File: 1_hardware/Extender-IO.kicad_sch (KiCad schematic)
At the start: 8 parts, among them U10 PCA9555PW,118, U11 PCA9555PW,118, U4 PCA9555PW,118, U5 PCA9555PW,118, U6 PCA9555PW,118, U7 PCA9555PW,118, U8 PCA9555PW,118, U9 PCA9555PW,118

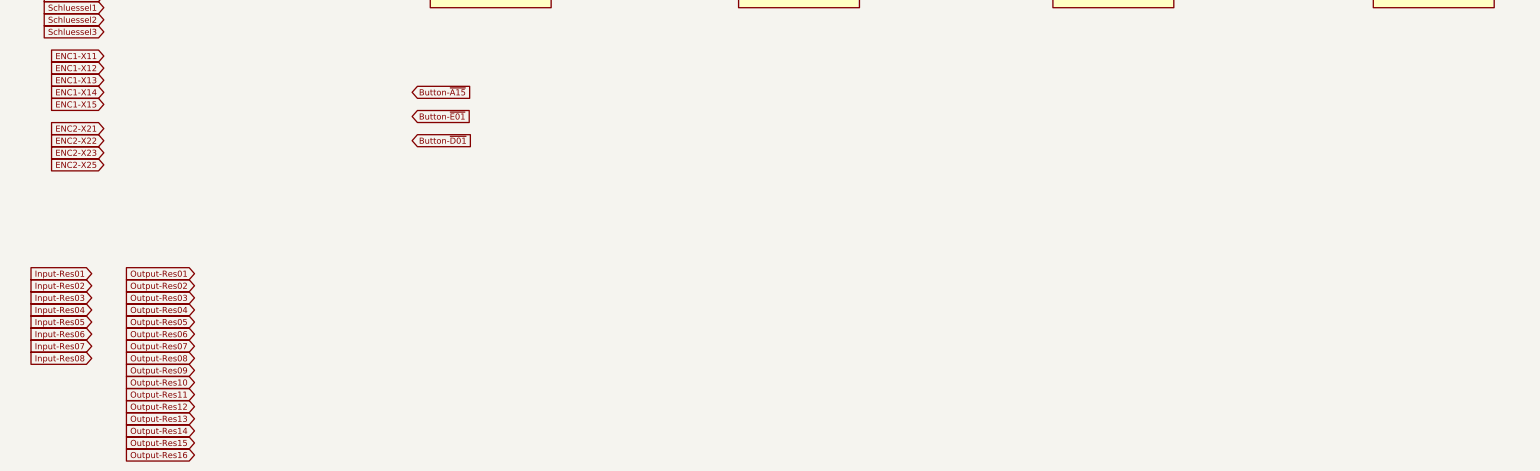
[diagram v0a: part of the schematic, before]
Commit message: finished most of schematic, init STM32 program
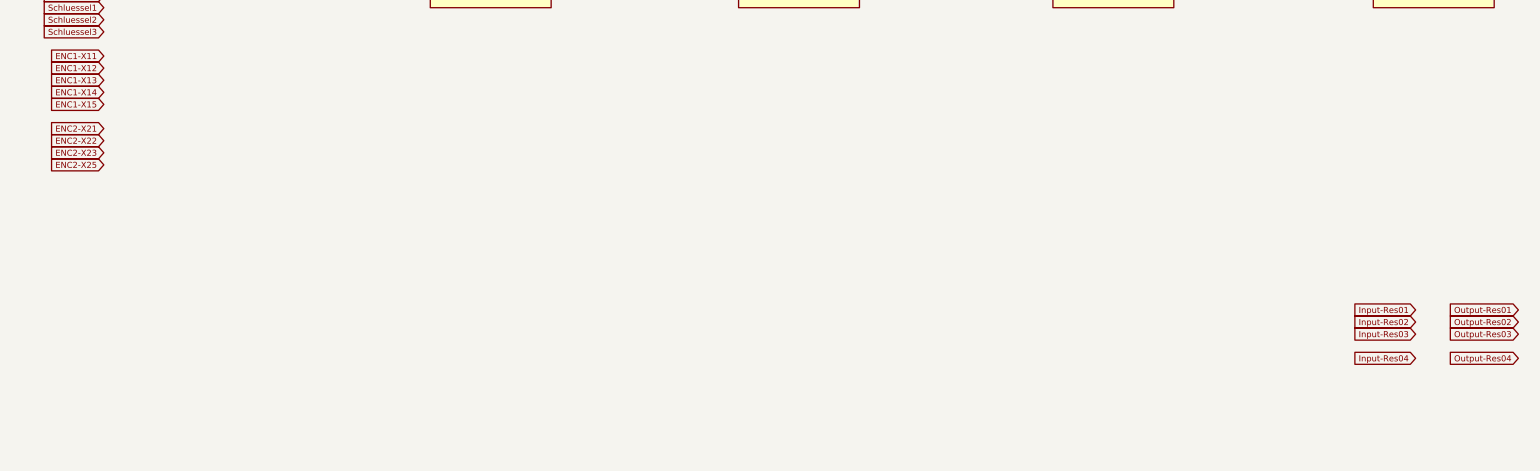
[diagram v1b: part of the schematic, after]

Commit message: finished schematics and board
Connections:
- net Button-A01: now also U9.10 (IO0_6)
- net Button-A02: now also U9.20 (IO1_7)
- net Button-A03: now also U9.19 (IO1_6)
- net Button-A04: now also U9.8 (IO0_4)
- net Button-A05: now also U9.17 (IO1_4)
- net Button-A06: now also U9.5 (IO0_1)
- net Button-A07: now also U9.6 (IO0_2)
- net Button-A08: now also U9.7 (IO0_3)
- net Button-A09: now also U9.9 (IO0_5)
- net Button-A10: now also U9.4 (IO0_0)
- net Button-A11: now also U9.11 (IO0_7)
- net Button-A12: now also U9.15 (IO1_2)
- net Button-A13: now also U10.17 (IO1_4)
- net Button-A14: now also U10.14 (IO1_1)
- net Button-A16: now also U10.5 (IO0_1)
- net Button-B01: now also U6.19 (IO1_6)
- net Button-B02: now also U6.18 (IO1_5)
- net Button-B03: now also U6.16 (IO1_3)
- net Button-B04: now also U6.14 (IO1_1)
- net Button-B05: now also U6.10 (IO0_6)
- net Button-B06: now also U6.8 (IO0_4)
- net Button-B07: now also U6.6 (IO0_2)
- net Button-B08: now also U6.4 (IO0_0)
- net Button-B09: now also U6.17 (IO1_4)
- net Button-B10: now also U6.15 (IO1_2)
- net Button-B11: now also U6.13 (IO1_0)
- net Button-B12: now also U6.11 (IO0_7)
- net Button-B13: now also U6.9 (IO0_5)
- net Button-B14: now also U6.7 (IO0_3)
- net Button-B15: now also U6.5 (IO0_1)
- net Button-C01: now also U5.10 (IO0_6)
- net Button-C02: now also U5.20 (IO1_7)
- net Button-C03: now also U5.19 (IO1_6)
- net Button-C04: now also U5.8 (IO0_4)
- net Button-C05: now also U5.17 (IO1_4)
- net Button-C06: now also U5.5 (IO0_1)
- net Button-C07: now also U5.6 (IO0_2)
- net Button-C08: now also U5.7 (IO0_3)
- net Button-C09: now also U5.9 (IO0_5)
- net Button-C10: now also U5.4 (IO0_0)
- net Button-C11: now also U5.11 (IO0_7)
- net Button-C12: now also U5.15 (IO1_2)
- net Button-C13: now also U5.16 (IO1_3)
- net Button-C14: now also U5.14 (IO1_1)
- net Button-C15: now also U5.18 (IO1_5)
- net Button-D02: now also U10.10 (IO0_6)
- net Button-E02: now also U10.8 (IO0_4)
- net ENC1-X11: now also U10.4 (IO0_0)
- net ENC1-X12: now also U10.6 (IO0_2)
- net ENC1-X13: now also U10.9 (IO0_5)
- net ENC1-X14: now also U10.11 (IO0_7)
- net ENC1-X15: now also U10.7 (IO0_3)
- net ENC2-X21: now also U9.13 (IO1_0)
- net ENC2-X22: now also U9.14 (IO1_1)
- net ENC2-X23: now also U9.18 (IO1_5)
- net ENC2-X25: now also U9.16 (IO1_3)
- net Input-Res01: now also U7.13 (IO1_0)
- net Input-Res02: now also U7.14 (IO1_1)
- net Input-Res03: now also U7.15 (IO1_2)
- net Input-Res04: now also U7.16 (IO1_3)
- net LED-A01: now also U8.7 (IO0_3)
- net LED-A02: now also U8.16 (IO1_3)
- net LED-A03: now also U8.15 (IO1_2)
- net LED-A04: now also U8.6 (IO0_2)
- net LED-A05: now also U8.14 (IO1_1)
- net LED-A06: now also U8.8 (IO0_4)
- net LED-A07: now also U8.5 (IO0_1)
- net LED-A08: now also U8.9 (IO0_5)
- net LED-A09: now also U8.10 (IO0_6)
- net LED-A10: now also U8.4 (IO0_0)
- net LED-A11: now also U8.11 (IO0_7)
- net LED-A12: now also U8.13 (IO1_0)
- net LED-A14: now also U11.6 (IO0_2)
- net LED-A15: now also U8.17 (IO1_4)
- net LED-A16: now also U8.18 (IO1_5)
- net LED-B01: now also U7.11 (IO0_7)
- net LED-B02: now also U7.10 (IO0_6)
- net LED-B03: now also U7.9 (IO0_5)
- net LED-B04: now also U7.8 (IO0_4)
- net LED-B05: now also U7.7 (IO0_3)
- net LED-B06: now also U7.6 (IO0_2)
- net LED-B07: now also U7.5 (IO0_1)
- net LED-B08: now also U7.4 (IO0_0)
- net LED-B09: now also U4.20 (IO1_7)
- net LED-B10: now also U4.19 (IO1_6)
- net LED-B11: now also U4.18 (IO1_5)
- net LED-B12: now also U4.17 (IO1_4)
- net LED-B13: now also U4.16 (IO1_3)
- net LED-B14: now also U4.15 (IO1_2)
- net LED-B15: now also U4.14 (IO1_1)
- net LED-C01: now also U11.10 (IO0_6)
- net LED-C02: now also U4.13 (IO1_0)
- net LED-C03: now also U4.11 (IO0_7)
- net LED-C04: now also U11.9 (IO0_5)
- net LED-C05: now also U4.10 (IO0_6)
- net LED-C06: now also U4.5 (IO0_1)
- net LED-C07: now also U11.8 (IO0_4)
- net LED-C08: now also U4.6 (IO0_2)
- net LED-C09: now also U4.7 (IO0_3)
- net LED-C10: now also U11.7 (IO0_3)
- net LED-C11: now also U4.8 (IO0_4)
- net LED-C12: now also U4.9 (IO0_5)
- net LED-C13: now also U11.11 (IO0_7)
- net LED-C15: now also U4.4 (IO0_0)
- net LED-D01: now also U11.4 (IO0_0)
- net LED-D02: now also U11.5 (IO0_1)
- net LED-E01: now also U8.19 (IO1_6)
- net LED-E02: now also U8.20 (IO1_7)
- net Output-Res01: now also U7.17 (IO1_4)
- net Output-Res02: now also U7.18 (IO1_5)
- net Output-Res03: now also U7.19 (IO1_6)
- net Output-Res04: now also U7.20 (IO1_7)
- net Schluessel0: now also U10.15 (IO1_2)
- net Schluessel1: now also U5.13 (IO1_0)
- net Schluessel2: now also U10.13 (IO1_0)
- net Schluessel3: now also U10.16 (IO1_3)
- net EXP_INT1: now reaches U4.1 (~{INT})
- net GND: now reaches U4.12 (VSS)
- net GND: now also U10.12 (VSS), U10.21 (A0), U10.3 (A2), U11.12 (VSS), U11.3 (A2), U4.2 (A1), U4.21 (A0), U5.12 (VSS), U5.2 (A1), U6.12 (VSS), U6.21 (A0), U7.12 (VSS), U8.12 (VSS), U8.2 (A1), U8.21 (A0), U8.3 (A2), U9.12 (VSS), U9.2 (A1), U9.3 (A2)
- net +3V3: now reaches U4.24 (VDD)
- net +3V3: now also U10.2 (A1), U10.24 (VDD), U11.2 (A1), U11.21 (A0), U11.24 (VDD), U4.3 (A2), U5.21 (A0), U5.24 (VDD), U5.3 (A2), U6.2 (A1), U6.24 (VDD), U6.3 (A2), U7.2 (A1), U7.21 (A0), U7.24 (VDD), U7.3 (A2), U8.24 (VDD), U9.21 (A0), U9.24 (VDD)
- net EXP_INT2: now reaches U5.1 (~{INT})
- net EXP_INT4: now reaches U7.1 (~{INT})
- net EXP_INT5: now reaches U8.1 (~{INT})
- net EXP_INT7: now reaches U10.1 (~{INT})
- net EXP_INT8: now reaches U11.1 (~{INT})
- net EXP_INT6: now reaches U9.1 (~{INT})
- net EXP_INT3: now reaches U6.1 (~{INT})
- no-connect marks 0 -> 12

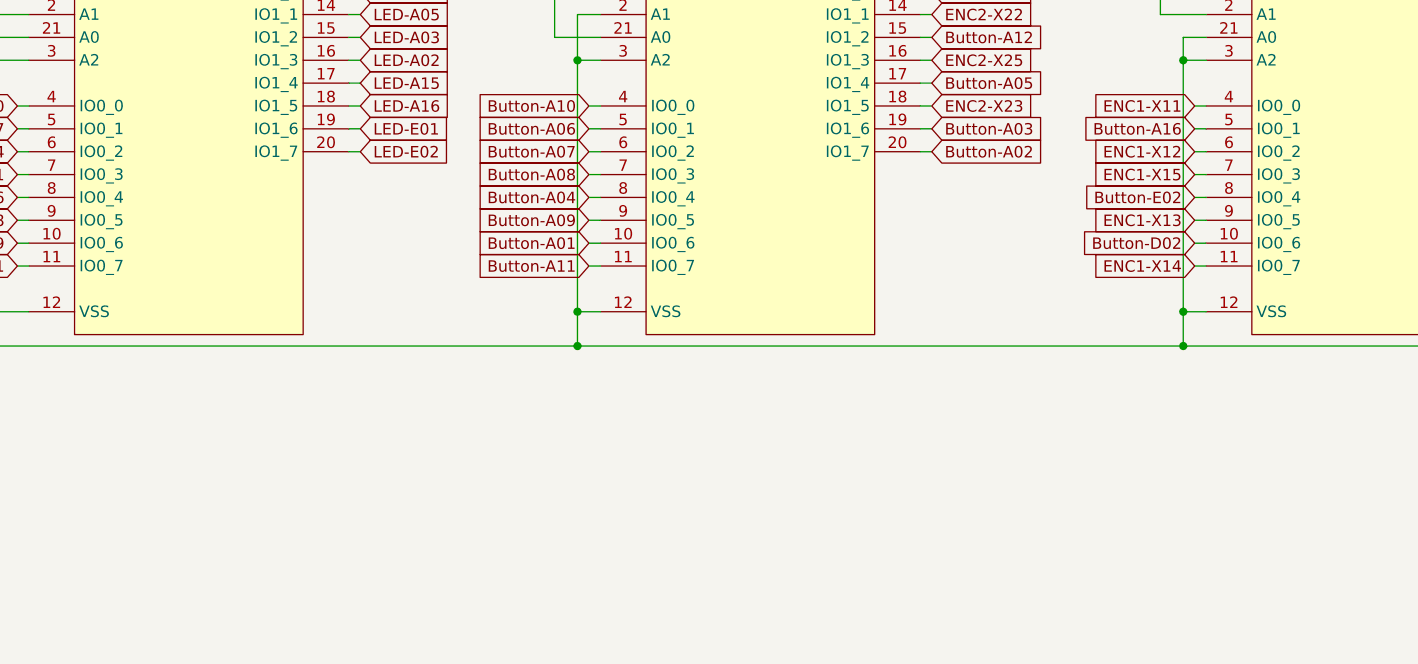
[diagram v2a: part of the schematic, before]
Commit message: changed from STM32F103C8 over to STM32L151C8 changed controller pinout, minor tweaks in board design, added labels and debug pads
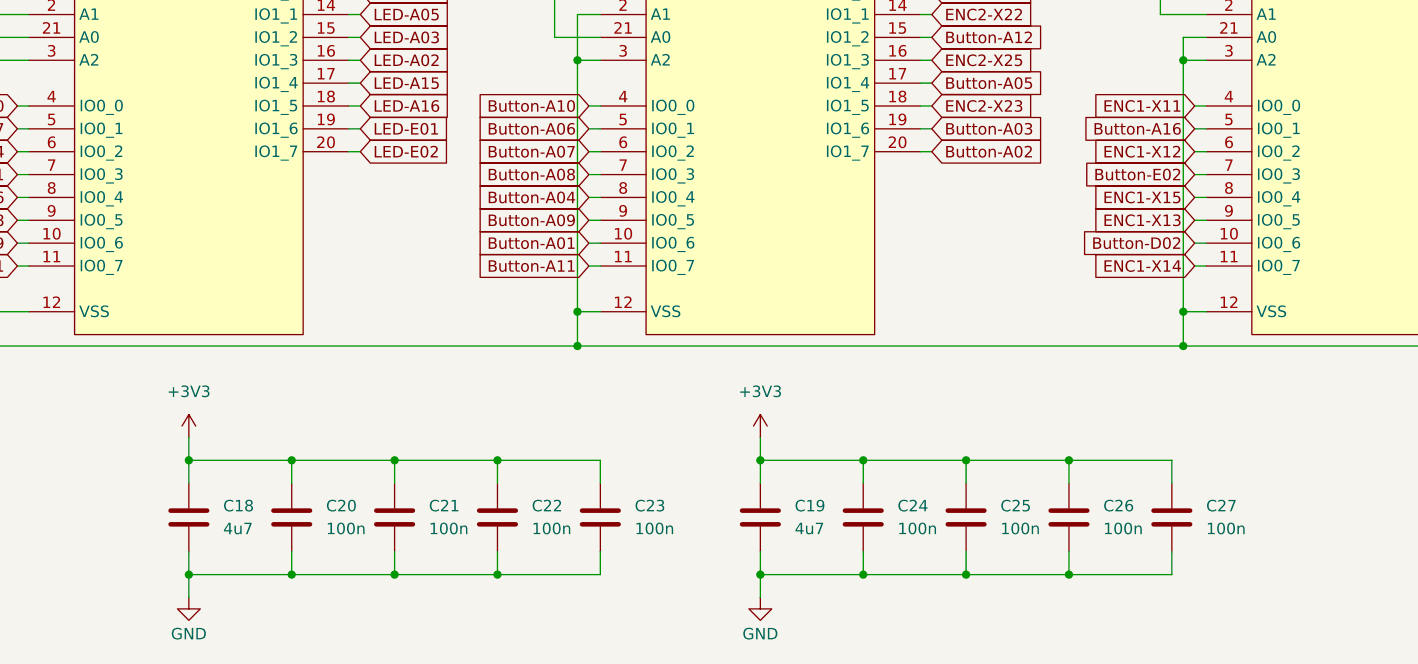
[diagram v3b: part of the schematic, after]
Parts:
- added C18, C19: 4u7, Capacitor_SMD:C_0603_1608Metric, symbol Device:C
- added C20, C21, C22, C23, C24, C25, C26, C27: 100n, Capacitor_SMD:C_0603_1608Metric, symbol Device:C
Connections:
- net +3V3: now also C18.2, C19.2, C20.2, C21.2, C22.2, C23.2, C24.2, C25.2, C26.2, C27.2
- net Button-E02: now also U10.7 (IO0_3); no longer U10.8 (IO0_4)
- net ENC1-X15: now also U10.8 (IO0_4); no longer U10.7 (IO0_3)
- net GND: now also C18.1, C19.1, C20.1, C21.1, C22.1, C23.1, C24.1, C25.1, C26.1, C27.1

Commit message: finished v0.9.2
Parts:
- renumbered C20 to C19, C21 to C20, C22 to C21, C23 to C22, C19 to C23
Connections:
- net Button-A13: now also U10.20 (IO1_7); no longer U10.17 (IO1_4)
- net Button-A14: now also U10.17 (IO1_4); no longer U10.14 (IO1_1)
- net Button-A16: now also U10.6 (IO0_2); no longer U10.5 (IO0_1)
- net Button-D02: now also U10.14 (IO1_1); no longer U10.10 (IO0_6)
- net Button-E02: now also U10.10 (IO0_6); no longer U10.7 (IO0_3)
- net ENC1-X11: now also U10.5 (IO0_1); no longer U10.4 (IO0_0)
- net ENC1-X12: now also U10.7 (IO0_3); no longer U10.6 (IO0_2)
- net ENC1-X13: now also U10.11 (IO0_7); no longer U10.9 (IO0_5)
- net ENC1-X14: now also U10.15 (IO1_2); no longer U10.11 (IO0_7)
- net ENC1-X15: now also U10.9 (IO0_5); no longer U10.8 (IO0_4)
- net Schluessel0: now also U10.18 (IO1_5); no longer U10.15 (IO1_2)
- net Schluessel2: now also U10.16 (IO1_3); no longer U10.13 (IO1_0)
- net Schluessel3: now also U10.19 (IO1_6); no longer U10.16 (IO1_3)
- net +3V3 renamed VCC
- new net Button-~{A15}: U10.4 (IO0_0)
- new net Button-~{D01}: U10.13 (IO1_0)
- new net Button-~{E01}: U10.8 (IO0_4)
- no-connect marks 12 -> 9

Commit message: PCB v0.9.4 - finished final prototype STM32 project reinitialised (F103C8 -> L151C8)
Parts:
- U10, U11, U4, U5, U6, U7, U8, U9: footprint easyeda2kicad:TSSOP-24_L7.8-W4.4-P0.65-LS6.4-BL -> project_library:TSSOP-24_L7.8-W4.4-P0.65-LS6.4-BL; symbol easyeda2kicad:PCA9555PW,118 -> project_library:PCA9555PW,118
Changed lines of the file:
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@@
 	(title_block
 		(title "Inputs/Outputs Extenders")
-		(date "2024-10-18")
-		(rev "v0.9.3")
+		(date "2024-10-20")
+		(rev "v0.9.4")
 	)
 	(junction
@@
 	)
 	(symbol
-		(lib_id "easyeda2kicad:PCA9555PW,118")
+		(lib_id "project_library:PCA9555PW,118")
 		(at 247.65 137.16 0)
 		(unit 1)
@@
 			)
 		)
-		(property "Footprint" "easyeda2kicad:TSSOP-24_L7.8-W4.4-P0.65-LS6.4-BL"
+		(property "Footprint" "project_library:TSSOP-24_L7.8-W4.4-P0.65-LS6.4-BL"
 			(at 247.65 166.37 0)
 			(effects
@@
 	)
 	(symbol
-		(lib_id "easyeda2kicad:PCA9555PW,118")
+		(lib_id "project_library:PCA9555PW,118")
 		(at 113.03 137.16 0)
 		(unit 1)
@@
 			)
 		)
-		(property "Footprint" "easyeda2kicad:TSSOP-24_L7.8-W4.4-P0.65-LS6.4-BL"
+		(property "Footprint" "project_library:TSSOP-24_L7.8-W4.4-P0.65-LS6.4-BL"
 			(at 113.03 166.37 0)
 			(effects
@@
 	)
 	(symbol
-		(lib_id "easyeda2kicad:PCA9555PW,118")
+		(lib_id "project_library:PCA9555PW,118")
 		(at 49.53 137.16 0)
 		(unit 1)
@@
 			)
 		)
-		(property "Footprint" "easyeda2kicad:TSSOP-24_L7.8-W4.4-P0.65-LS6.4-BL"
+		(property "Footprint" "project_library:TSSOP-24_L7.8-W4.4-P0.65-LS6.4-BL"
 			(at 49.53 166.37 0)
 			(effects
@@
 	)
 	(symbol
-		(lib_id "easyeda2kicad:PCA9555PW,118")
+		(lib_id "project_library:PCA9555PW,118")
 		(at 180.34 60.96 0)
 		(unit 1)
@@
 			)
 		)
-		(property "Footprint" "easyeda2kicad:TSSOP-24_L7.8-W4.4-P0.65-LS6.4-BL"
+		(property "Footprint" "project_library:TSSOP-24_L7.8-W4.4-P0.65-LS6.4-BL"
 			(at 180.34 90.17 0)
 			(effects
@@
 	)
 	(symbol
-		(lib_id "easyeda2kicad:PCA9555PW,118")
+		(lib_id "project_library:PCA9555PW,118")
 		(at 49.53 60.96 0)
 		(unit 1)
@@
 			)
 		)
-		(property "Footprint" "easyeda2kicad:TSSOP-24_L7.8-W4.4-P0.65-LS6.4-BL"
+		(property "Footprint" "project_library:TSSOP-24_L7.8-W4.4-P0.65-LS6.4-BL"
 			(at 49.53 90.17 0)
 			(effects
@@
 	)
 	(symbol
-		(lib_id "easyeda2kicad:PCA9555PW,118")
+		(lib_id "project_library:PCA9555PW,118")
 		(at 113.03 60.96 0)
 		(unit 1)
@@
 			)
 		)
-		(property "Footprint" "easyeda2kicad:TSSOP-24_L7.8-W4.4-P0.65-LS6.4-BL"
+		(property "Footprint" "project_library:TSSOP-24_L7.8-W4.4-P0.65-LS6.4-BL"
 			(at 113.03 90.17 0)
 			(effects
@@
 	)
 	(symbol
-		(lib_id "easyeda2kicad:PCA9555PW,118")
+		(lib_id "project_library:PCA9555PW,118")
 		(at 247.65 60.96 0)
 		(unit 1)
@@
 			)
 		)
-		(property "Footprint" "easyeda2kicad:TSSOP-24_L7.8-W4.4-P0.65-LS6.4-BL"
+		(property "Footprint" "project_library:TSSOP-24_L7.8-W4.4-P0.65-LS6.4-BL"
 			(at 247.65 90.17 0)
 			(effects
@@
 	)
 	(symbol
-		(lib_id "easyeda2kicad:PCA9555PW,118")
+		(lib_id "project_library:PCA9555PW,118")
 		(at 180.34 137.16 0)
 		(unit 1)
@@
 			)
 		)
-		(property "Footprint" "easyeda2kicad:TSSOP-24_L7.8-W4.4-P0.65-LS6.4-BL"
+		(property "Footprint" "project_library:TSSOP-24_L7.8-W4.4-P0.65-LS6.4-BL"
 			(at 180.34 166.37 0)
 			(effects
